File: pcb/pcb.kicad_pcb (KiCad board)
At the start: 2 copper layers, 163.6 x 116.9 mm, 86 parts, among them J1 USB-Mini, J2 Conn_01x04, P1 i2c-pin1, P2 i2c-pin2, SW1 SW_Push, SW10 SW_Push, SW11 SW_Push, SW12 SW_Push, SW13 SW_Push, SW14 SW_Push, SW15 SW_Push, SW16 SW_Push, SW17 SW_Push, SW18 SW_Push, SW19 SW_Push, SW2 SW_Push, SW20 SW_Push, SW21 SW_Push, SW22 SW_Push, SW23 SW_Push, SW24 SW_Push, SW25 SW_Push, SW26 SW_Push, SW27 SW_Push, SW28 SW_Push, SW29 SW_Push, SW3 SW_Push, SW30 SW_Push, SW31 SW_Push, SW32 SW_Push, SW33 SW_Push, SW34 SW_Push, SW35 SW_Push, SW36 SW_Push, SW37 SW_Push, SW38 SW_Push, SW39 SW_Push, SW4 SW_Push, SW40 SW_Push, SW5 SW_Push, SW6 SW_Push, SW7 SW_Push, SW8 SW_Push, SW9 SW_Push, U1 ProMicro, U2 TRRS

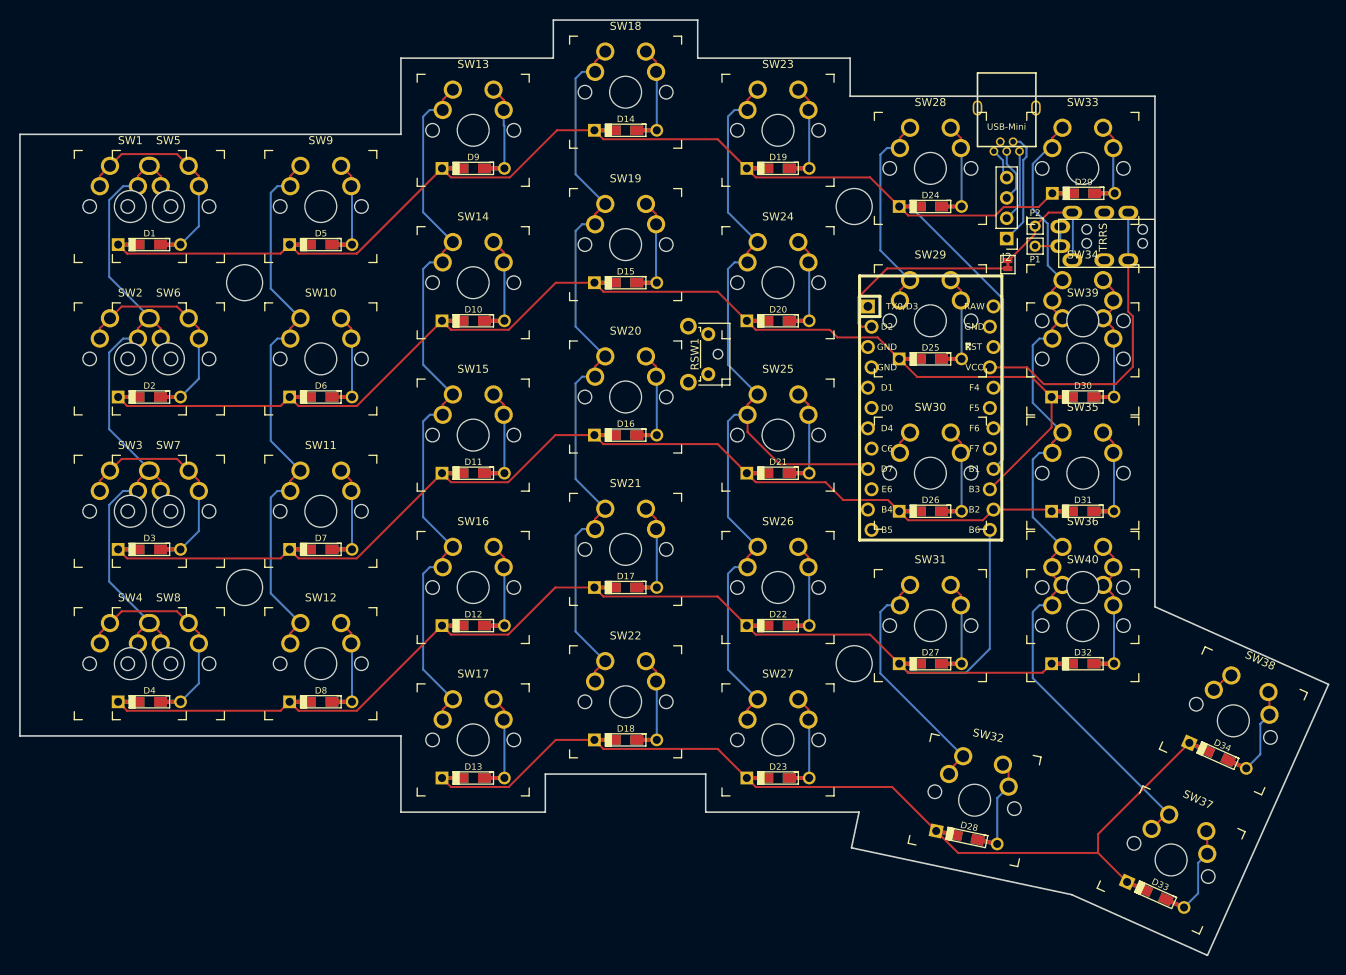
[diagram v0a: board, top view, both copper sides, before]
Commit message: finished case and pcb prototype
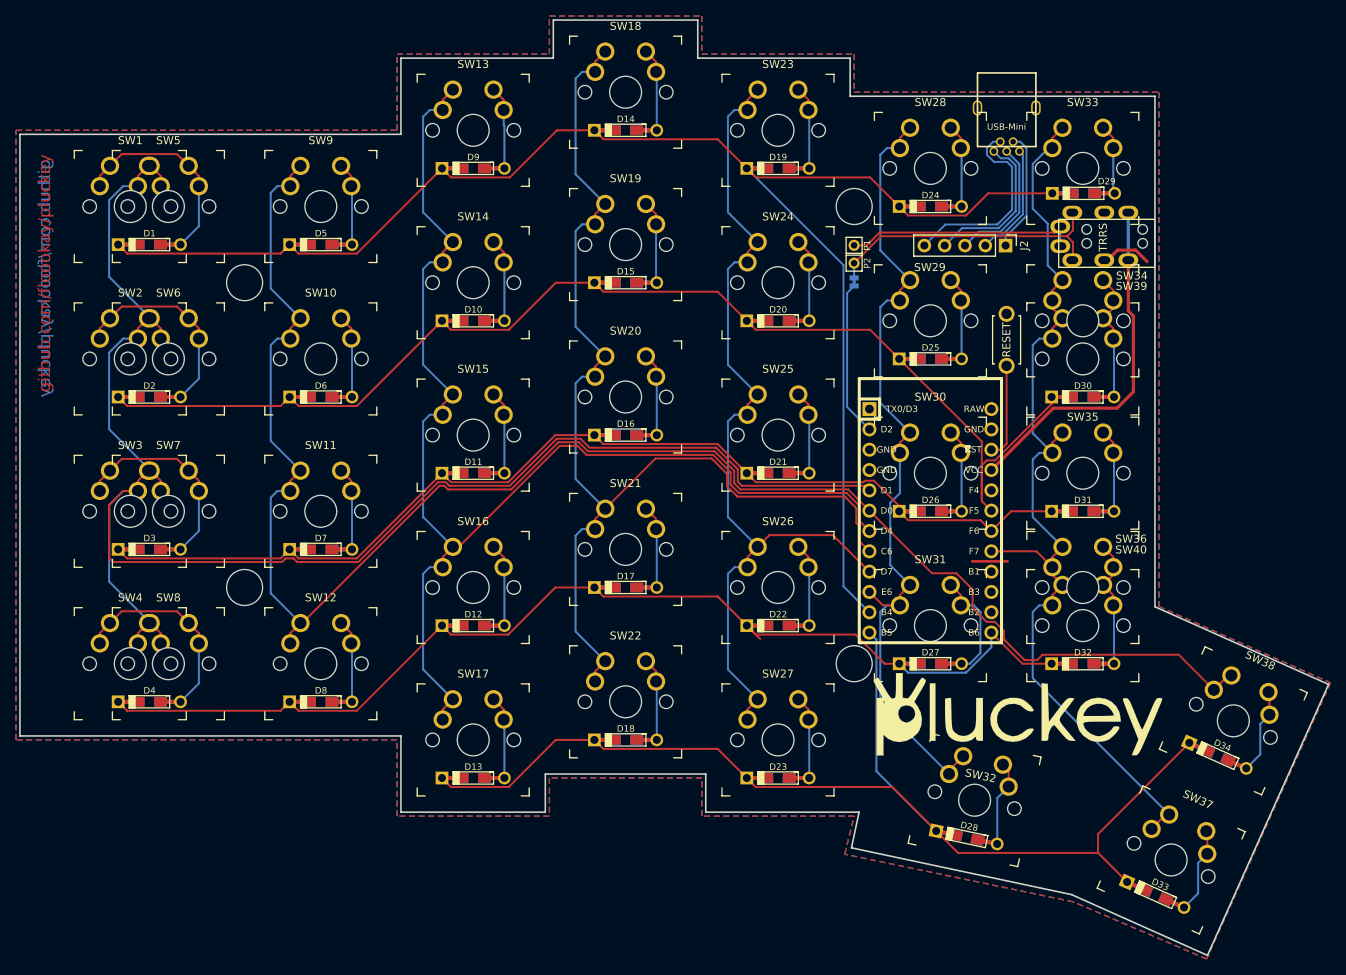
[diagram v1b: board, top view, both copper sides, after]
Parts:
- added G***: LOGO, local:pluckey_logo, F.Cu at (149.1, 146.8)
- added G***: LOGO, local:pluckey_logo, B.Cu at (147.1, 146.8)
- J2: value Conn_01x04 -> Conn_01x05; footprint Connector_PinHeader_2.54mm:PinHeader_1x04_P2.54mm_Vertical -> Connector_PinHeader_2.54mm:PinHeader_1x05_P2.54mm_Vertical
- JP1: moved to B.Cu
- RSW1: footprint Keebio-Parts:SW_Tactile_SPST_Angled_MJTP1117 -> kbd:ResetSW
- U1: footprint Keebio-Parts:ArduinoProMicro-ZigZag -> Keebio-Parts:ArduinoProMicro
- moved RSW1 37.3 mm to (147.6, 100.0)
- moved P2 23.1 mm to (128.6, 90.4), turned to 90 degrees
- moved P1 22.6 mm to (128.6, 88.2), turned to 90 degrees
- moved JP1 19.3 mm to (128.6, 92.8)
- moved U1 12.8 mm to (138.1, 122.6)
- moved J2 0.89 mm to (147.5, 88.2), turned to 270 degrees
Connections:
- U1 pad 11: /col6 -> /row0
- U1 pad 14: /row2 -> Net-(U1-Pad14)
- U1 pad 15: /row1 -> Net-(U1-Pad15)
- U1 pad 16: /row0 -> Net-(U1-Pad16)
- U1 pad 17: Net-(U1-Pad17) -> /col6
- U1 pad 18: Net-(U1-Pad18) -> /row2
- U1 pad 19: Net-(U1-Pad19) -> /row1
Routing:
- net /col1: track 75.2 -> 215.4 mm
- net /col0: track 88.2 -> 205.1 mm
- net /col2: track 95.4 -> 159.1 mm
- net /col5: track 60.3 -> 104.4 mm
- net /col3: track 95.4 -> 138.9 mm
- net /row4: track 114.4 -> 142.6 mm
- net Net-(J1-Pad4): track 0.00 -> 24.8 mm
- net Net-(P1-Pad1): track 5.60 -> 30.1 mm
- net /row0: track 170.5 -> 194.3 mm
- net /row3: track 158.2 -> 137.0 mm
- net Net-(JP1-Pad2): track 17.1 -> 36.7 mm
- net Net-(J1-Pad5): track 3.94 -> 19.8 mm
- net /reset: track 0.00 -> 12.0 mm
- net GND: track 0.00 -> 10.9 mm
- net /col6: track 111.9 -> 122.5 mm
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- added copper zone on B.Cu, net GND
- added copper zone on F.Cu, net GND
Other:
- net class GND added: clearance 0.2, trace_width 0.4, via_dia 0.8, via_drill 0.4
- net class VCC added: clearance 0.2, trace_width 0.4, via_dia 0.8, via_drill 0.4
- board text added: "github.com/floookay/pluckey"

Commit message: finalised pcb rev1.1
added support for an encoder
added support for a stablized 2u key on the double thumb keys
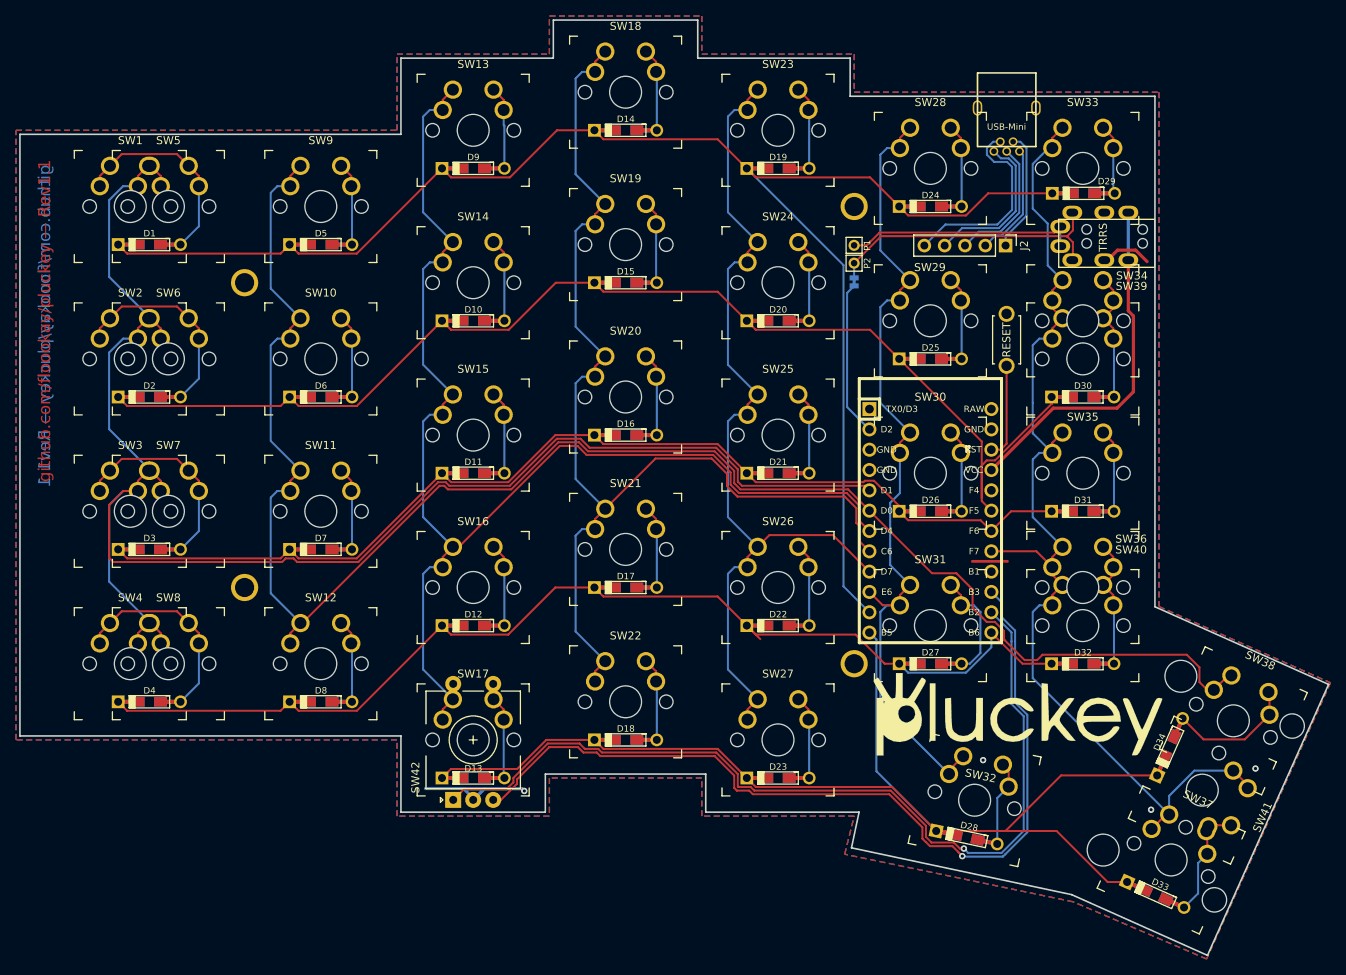
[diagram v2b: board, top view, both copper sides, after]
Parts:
- added REF**: Stabilizer_MX_2u, keyswitches:Stabilizer_MX_2u, F.Cu at (172.1, 156.3)
- added SW41: SW_Push, keyswitches:SW_MX_reversible, F.Cu at (172.1, 156.3)
- added SW42: Rotary_Encoder_Switch, local:RotaryEncoder_Alps_EC11E-Switch_Vertical_H20mm, F.Cu at (81.0, 150.0)
- H1, H2, H3, H4: footprint local:m4.5_hole -> local:m2.4_hole_plated
- moved D34 6.09 mm to (168.1, 150.9), turned to 245.9 degrees
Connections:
- U1 pad 14: Net-(U1-Pad14) -> /re1
- U1 pad 15: Net-(U1-Pad15) -> /re0
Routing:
- net /re1: track 0.00 -> 112.1 mm, vias 0 -> 1
- net /re0: track 0.00 -> 110.8 mm, vias 0 -> 1
- net GND: track 10.9 -> 27.2 mm, vias 0 -> 4
- net /col6: track 122.5 -> 137.2 mm
- net Net-(D34-Pad2): track 10.8 -> 16.1 mm
- net /row4: track 142.6 -> 147.3 mm
- net Net-(D33-Pad2): track 10.8 -> 13.7 mm
- net Net-(D13-Pad2): track 10.4 -> 12.4 mm
- net /col2: track 159.1 -> 161.0 mm
- net /col1: track 215.4 -> 216.5 mm
- net (no net): track 0.00 -> 0.70 mm
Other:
- board text added: "github.com/floookay/pluckey — Rev1.1"
- board text removed: "github.com/floookay/pluckey"

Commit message: updated silkscreen text
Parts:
- J2: footprint Connector_PinHeader_2.54mm:PinHeader_1x05_P2.54mm_Vertical -> local:PinHeader_1x05_P2.54mm_Vertical
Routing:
- net /row3: track 137.0 -> 134.6 mm
- net /re1: track 112.1 -> 113.0 mm
- net /re0: track 110.8 -> 111.7 mm
- net Net-(J1-Pad1): track 14.4 -> 15.2 mm
- net Net-(J1-Pad3): track 16.8 -> 17.5 mm
- net GND: vias 4 -> 5
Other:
- net class thick_header added: clearance 0.2, trace_width 0.4, via_dia 0.8, via_drill 0.4
